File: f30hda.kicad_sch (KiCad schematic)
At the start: 9 parts, among them J1 USB3_A, J2 USB3_A, J3 Conn_01x10, J4 Conn_01x10, J5 PJ-343, J6 PJ-343, J7 Conn_02x05_Odd_Even, J8 Conn_01x06_Pin, J9 USB_A_Stacked

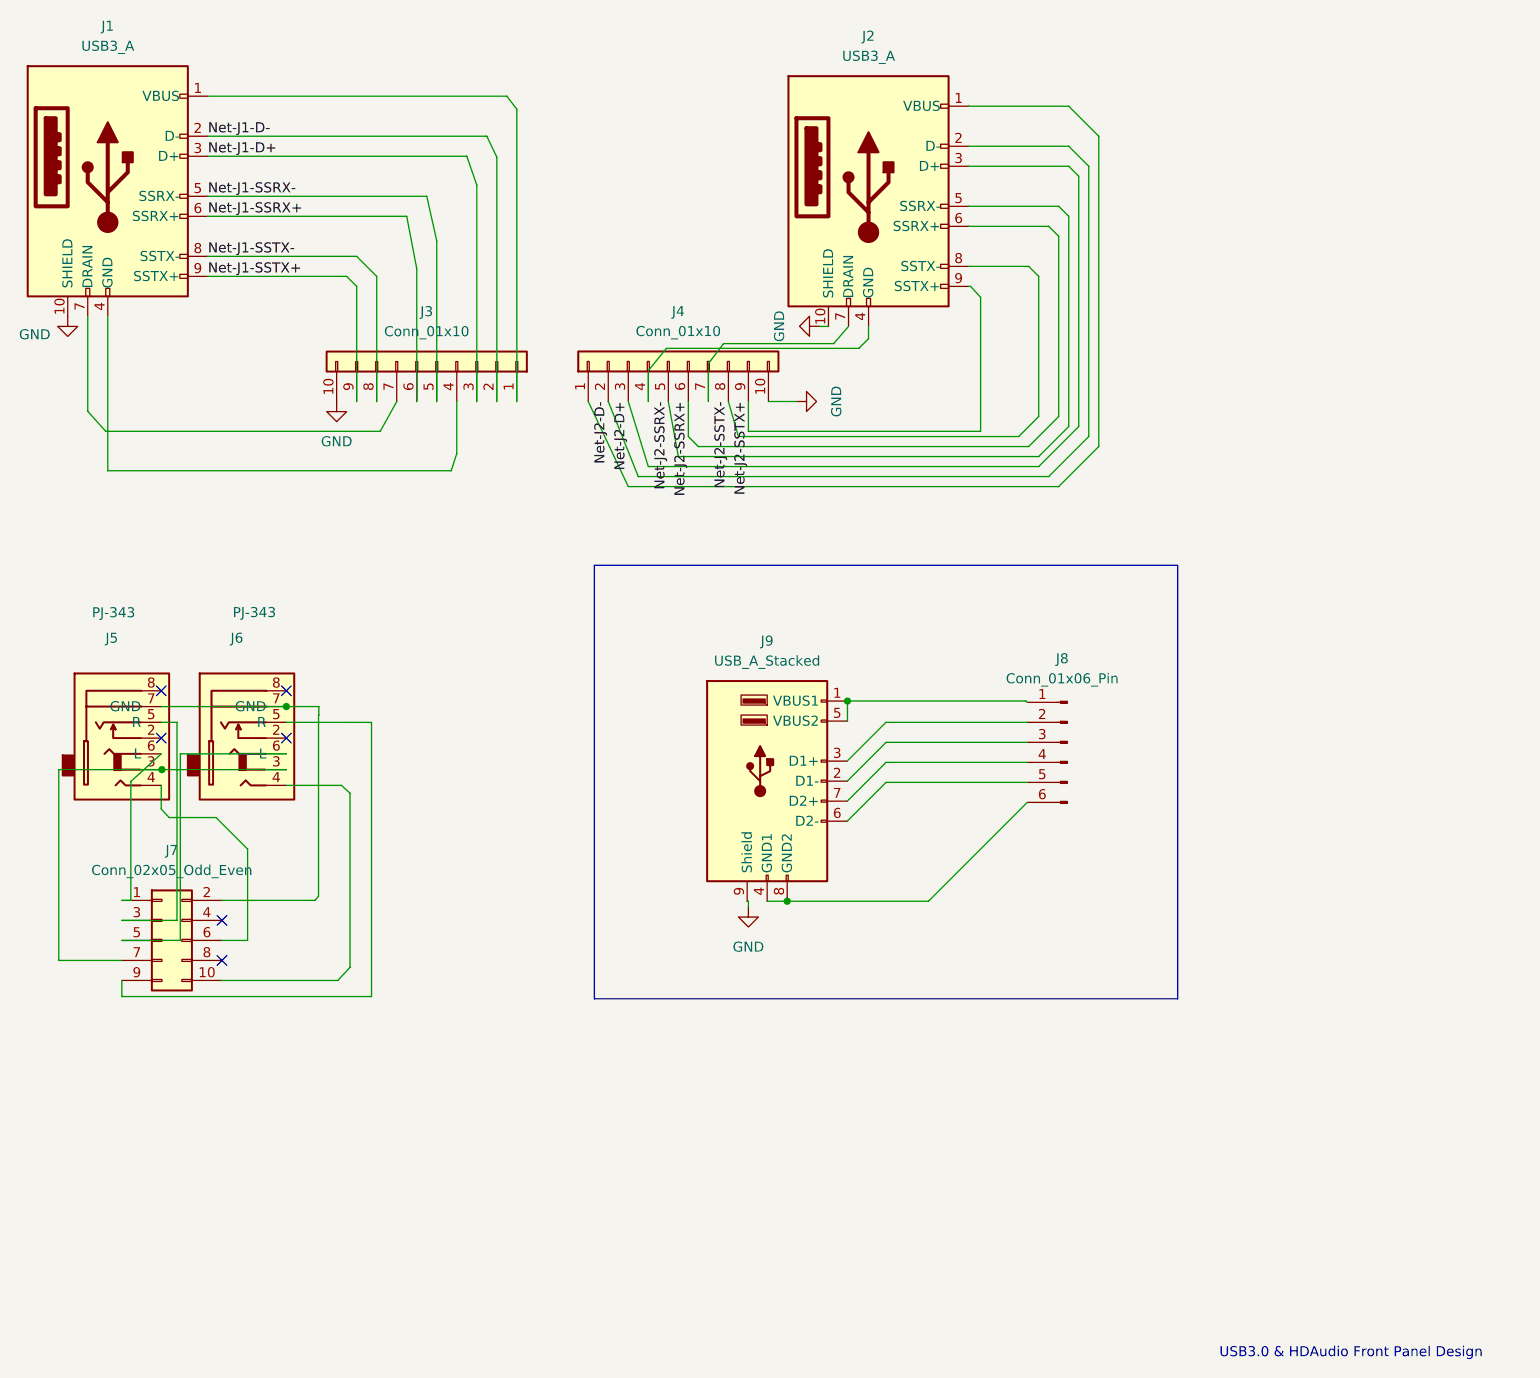
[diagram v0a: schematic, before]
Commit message: add required logo
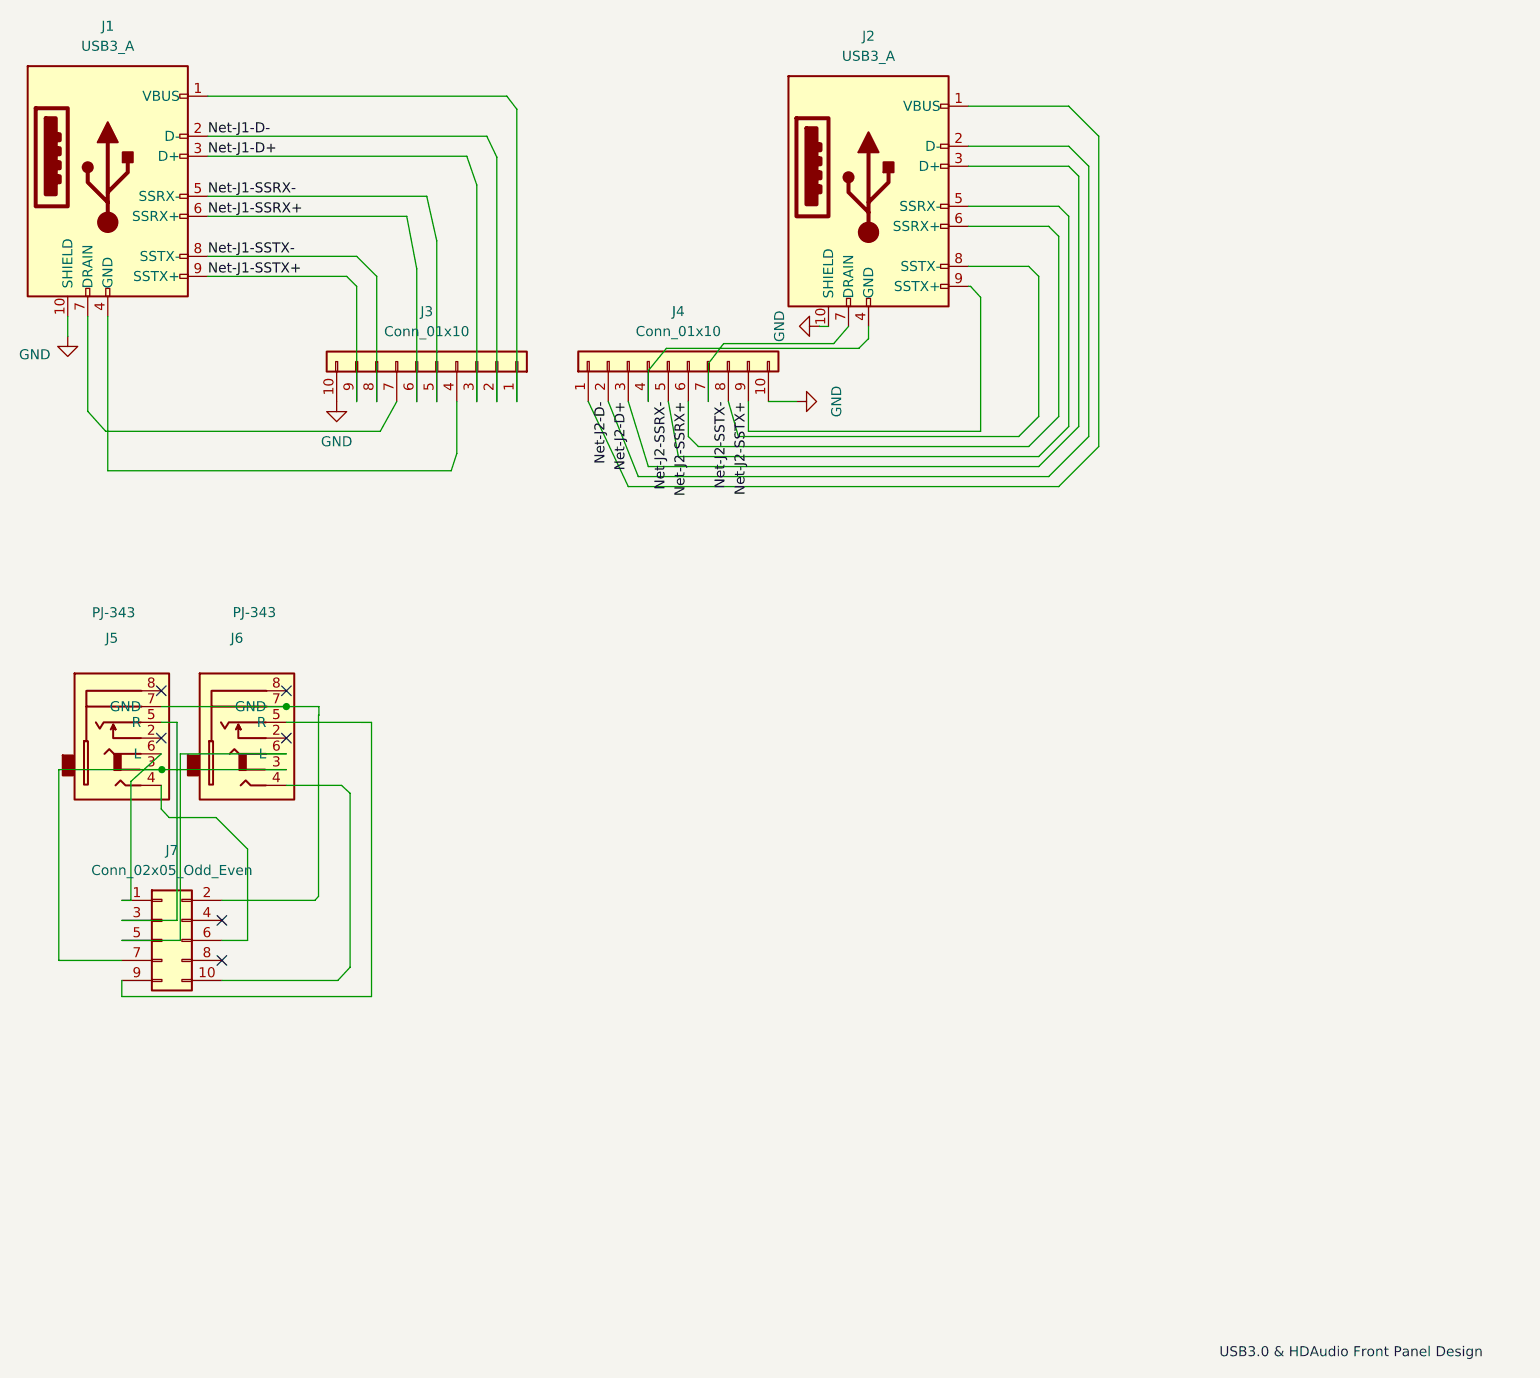
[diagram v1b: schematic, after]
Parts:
- removed J8: Conn_01x06_Pin, Connector_PinHeader_1.00mm:PinHeader_1x06_P1.00mm_Vertical, symbol Connector:Conn_01x06_Pin
- removed J9: USB_A_Stacked, Connector_USB:USB_A_Wuerth_61400826021_Horizontal_Stacked, symbol Connector:USB_A_Stacked
